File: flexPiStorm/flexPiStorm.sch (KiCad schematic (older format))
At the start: 9 parts, among them J1 Conn_01x04, J2 FPC-FFC-64, U1 MC68000

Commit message: Added LOGOs in the schematics, so the PCB will have them already. Run DRC for errors. Report only three (3) overlap for silkscreen and filled zones. No problem at all.
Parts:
- added L1: GNU GPL LOGO, RetroBitLab:Symbol_GNU-GPL_SilkScreen_Small, symbol AmigaComponents:LOGO
- added L2: KiCad LOGO Design, Symbol:KiCad-Logo2_6mm_SilkScreen, symbol AmigaComponents:LOGO
- added L3: PiStorm LOGO Design, RetroBitLab:PiStorm_32x6-NEG, symbol AmigaComponents:LOGO
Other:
- note added: "FLOPPY HEADER MOLEX 4 PIN CONNECTOR TYPE"
- note added: "LOGO FOR SILKSCREEN"
- note added: "MOUNTING HOLES 3.2mm"
- moved on the sheet: H1, H2, H3, H4
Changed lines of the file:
@@
 Sheet 1 1
 Title "Secondary CPU Flexible Relocator"
-Date "2021-06-25"
-Rev "0.1"
+Date "2021-06-27"
+Rev "0.2"
 Comp "RETROBIT LAB"
 Comment1 "FlexPiStorm"
@@
 L Mechanical:MountingHole H1
 U 1 1 60E64491
-P 8350 1550
-F 0 "H1" H 8450 1600 50  0000 L CNN
-F 1 "MountingHole" H 8450 1550 50  0000 L CNN
-F 2 "MountingHole:MountingHole_3.2mm_M3" H 8350 1550 50  0001 C CNN
-F 3 "~" H 8350 1550 50  0001 C CNN
-	1    8350 1550
-	1    0    0    -1
+P 9400 1500
+F 0 "H1" H 9500 1550 50  0000 L CNN
+F 1 "MountingHole" H 9500 1500 50  0000 L CNN
+F 2 "MountingHole:MountingHole_3.2mm_M3" H 9400 1500 50  0001 C CNN
+F 3 "~" H 9400 1500 50  0001 C CNN
+	1    9400 1500
+	0    -1   -1   0
 $EndComp
 $Comp
 L Mechanical:MountingHole H2
 U 1 1 60E64C09
-P 8350 1850
-F 0 "H2" H 8450 1900 50  0000 L CNN
-F 1 "MountingHole" H 8450 1850 50  0000 L CNN
-F 2 "MountingHole:MountingHole_3.2mm_M3" H 8350 1850 50  0001 C CNN
-F 3 "~" H 8350 1850 50  0001 C CNN
-	1    8350 1850
-	1    0    0    -1
+P 9700 1500
+F 0 "H2" H 9800 1550 50  0000 L CNN
+F 1 "MountingHole" H 9800 1500 50  0000 L CNN
+F 2 "MountingHole:MountingHole_3.2mm_M3" H 9700 1500 50  0001 C CNN
+F 3 "~" H 9700 1500 50  0001 C CNN
+	1    9700 1500
+	0    -1   -1   0
 $EndComp
 $Comp
 L Mechanical:MountingHole H3
 U 1 1 60E64DD7
-P 8350 2150
-F 0 "H3" H 8450 2200 50  0000 L CNN
-F 1 "MountingHole" H 8450 2150 50  0000 L CNN
-F 2 "MountingHole:MountingHole_3.2mm_M3" H 8350 2150 50  0001 C CNN
-F 3 "~" H 8350 2150 50  0001 C CNN
-	1    8350 2150
-	1    0    0    -1
+P 10000 1500
+F 0 "H3" H 10100 1550 50  0000 L CNN
+F 1 "MountingHole" H 10100 1500 50  0000 L CNN
+F 2 "MountingHole:MountingHole_3.2mm_M3" H 10000 1500 50  0001 C CNN
+F 3 "~" H 10000 1500 50  0001 C CNN
+	1    10000 1500
+	0    -1   -1   0
 $EndComp
 $Comp
 L Mechanical:MountingHole H4
 U 1 1 60E65040
-P 8350 2500
-F 0 "H4" H 8450 2550 50  0000 L CNN
-F 1 "MountingHole" H 8450 2500 50  0000 L CNN
-F 2 "MountingHole:MountingHole_3.2mm_M3" H 8350 2500 50  0001 C CNN
-F 3 "~" H 8350 2500 50  0001 C CNN
-	1    8350 2500
-	1    0    0    -1
+P 10350 1500
+F 0 "H4" H 10450 1550 50  0000 L CNN
+F 1 "MountingHole" H 10450 1500 50  0000 L CNN
+F 2 "MountingHole:MountingHole_3.2mm_M3" H 10350 1500 50  0001 C CNN
+F 3 "~" H 10350 1500 50  0001 C CNN
+	1    10350 1500
+	0    -1   -1   0
 $EndComp
 $Comp
@@
 Wire Wire Line
 	1150 3200 2000 3200
+Wire Notes Line
+	9050 800  9050 1750
+Wire Notes Line
+	9050 1750 10550 1750
+Wire Notes Line
+	10550 1750 10550 800
+Wire Notes Line
+	10550 800  9050 800
+Text Notes 9050 1900 0    79   ~ 16
+MOUNTING HOLES 3.2mm
+$Comp
+L AmigaComponents:LOGO L1
+U 1 1 60D96003
+P 9000 2550
+F 0 "L1" H 9150 2650 59  0000 L CNN
+F 1 "GNU GPL LOGO" H 9150 2500 59  0000 L CNN
+F 2 "RetroBitLab:Symbol_GNU-GPL_SilkScreen_Small" H 9000 2550 59  0001 C CNN
+F 3 "" H 9000 2550 59  0001 C CNN
+	1    9000 2550
+	1    0    0    -1
+$EndComp
+$Comp
+L AmigaComponents:LOGO L2
+U 1 1 60D96862
+P 9000 2850
+F 0 "L2" H 9150 2950 59  0000 L CNN
+F 1 "KiCad LOGO Design" H 9150 2800 59  0000 L CNN
+F 2 "Symbol:KiCad-Logo2_6mm_SilkScreen" H 9000 2850 59  0001 C CNN
+F 3 "" H 9000 2850 59  0001 C CNN
+	1    9000 2850
+	1    0    0    -1
+$EndComp
+$Comp
+L AmigaComponents:LOGO L3
+U 1 1 60D96C34
+P 9000 3150
+F 0 "L3" H 9150 3250 59  0000 L CNN
+F 1 "PiStorm LOGO Design" H 9150 3100 59  0000 L CNN
+F 2 "RetroBitLab:PiStorm_32x6-NEG" H 9000 3150 59  0001 C CNN
+F 3 "" H 9000 3150 59  0001 C CNN
+	1    9000 3150
+	1    0    0    -1
+$EndComp
+Wire Notes Line
+	9050 2300 9050 3350
+Wire Notes Line
+	9050 3350 10550 3350
+Wire Notes Line
+	10550 3350 10550 2300
+Wire Notes Line
+	10550 2300 9050 2300
+Text Notes 9050 3500 0    79   ~ 16
+LOGO FOR SILKSCREEN
+Text Notes 750  3700 0    79   ~ 16
+FLOPPY HEADER MOLEX 4 PIN CONNECTOR TYPE
 $EndSCHEMATC

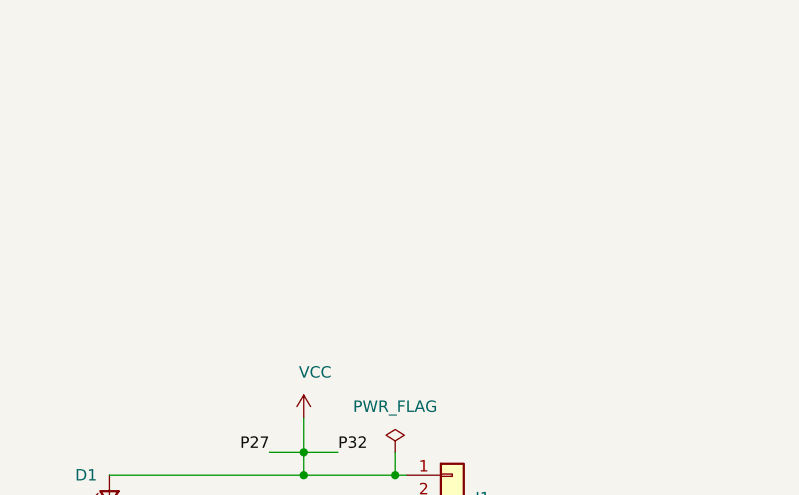
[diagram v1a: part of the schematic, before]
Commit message: Added bypass capacitors 10000pF Ceramics 1206 HandSolder
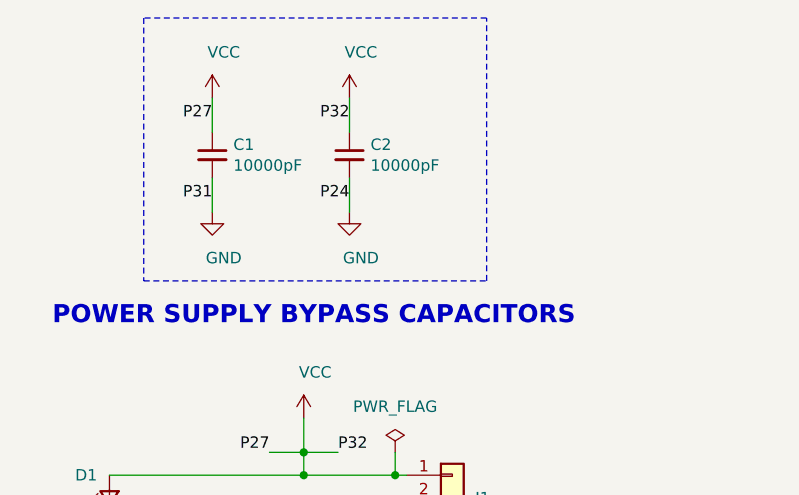
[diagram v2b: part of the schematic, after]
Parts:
- added C1, C2: 10000pF, Capacitor_SMD:C_1206_3216Metric_Pad1.33x1.80mm_HandSolder, symbol Device:C_Small
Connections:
- net GND: now also C1.2, C2.2
- net VCC: now also C1.1, C2.1
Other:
- note added: "POWER SUPPLY BYPASS CAPACITORS"
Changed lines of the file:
@@
 Sheet 1 1
 Title "Secondary CPU Flexible Relocator"
-Date "2021-06-27"
-Rev "0.2"
+Date "2021-06-28"
+Rev "0.3"
 Comp "RETROBIT LAB"
 Comment1 "FlexPiStorm"
@@
 Text Notes 750  3700 0    79   ~ 16
 FLOPPY HEADER MOLEX 4 PIN CONNECTOR TYPE
+$Comp
+L Device:C_Small C1
+U 1 1 60DA364B
+P 1600 1300
+F 0 "C1" H 1692 1346 50  0000 L CNN
+F 1 "10000pF" H 1692 1255 50  0000 L CNN
+F 2 "Capacitor_SMD:C_1206_3216Metric_Pad1.33x1.80mm_HandSolder" H 1600 1300 50  0001 C CNN
+F 3 "~" H 1600 1300 50  0001 C CNN
+	1    1600 1300
+	1    0    0    -1
+$EndComp
+Text Label 1600 1150 2    50   ~ 0
+P27
+Text Label 1600 1500 2    50   ~ 0
+P31
+$Comp
+L power:GND #PWR04
+U 1 1 60DA402B
+P 1600 1550
+F 0 "#PWR04" H 1600 1300 50  0001 C CNN
+F 1 "GND" H 1650 1350 50  0000 C CNN
+F 2 "" H 1600 1550 50  0001 C CNN
+F 3 "" H 1600 1550 50  0001 C CNN
+	1    1600 1550
+	1    0    0    -1
+$EndComp
+$Comp
+L power:VCC #PWR03
+U 1 1 60DA440B
+P 1600 1050
+F 0 "#PWR03" H 1600 900 50  0001 C CNN
+F 1 "VCC" H 1650 1250 50  0000 C CNN
+F 2 "" H 1600 1050 50  0001 C CNN
+F 3 "" H 1600 1050 50  0001 C CNN
+	1    1600 1050
+	1    0    0    -1
+$EndComp
+Wire Wire Line
+	1600 1050 1600 1200
+Wire Wire Line
+	1600 1400 1600 1550
+$Comp
+L Device:C_Small C2
+U 1 1 60DC5962
+P 2200 1300
+F 0 "C2" H 2292 1346 50  0000 L CNN
+F 1 "10000pF" H 2292 1255 50  0000 L CNN
+F 2 "Capacitor_SMD:C_1206_3216Metric_Pad1.33x1.80mm_HandSolder" H 2200 1300 50  0001 C CNN
+F 3 "~" H 2200 1300 50  0001 C CNN
+	1    2200 1300
+	1    0    0    -1
+$EndComp
+Text Label 2200 1150 2    50   ~ 0
+P32
+Text Label 2200 1500 2    50   ~ 0
+P24
+$Comp
+L power:GND #PWR06
+U 1 1 60DC5A8A
+P 2200 1550
+F 0 "#PWR06" H 2200 1300 50  0001 C CNN
+F 1 "GND" H 2250 1350 50  0000 C CNN
+F 2 "" H 2200 1550 50  0001 C CNN
+F 3 "" H 2200 1550 50  0001 C CNN
+	1    2200 1550
+	1    0    0    -1
+$EndComp
+$Comp
+L power:VCC #PWR05
+U 1 1 60DC5A94
+P 2200 1050
+F 0 "#PWR05" H 2200 900 50  0001 C CNN
+F 1 "VCC" H 2250 1250 50  0000 C CNN
+F 2 "" H 2200 1050 50  0001 C CNN
+F 3 "" H 2200 1050 50  0001 C CNN
+	1    2200 1050
+	1    0    0    -1
+$EndComp
+Wire Wire Line
+	2200 1050 2200 1200
+Wire Wire Line
+	2200 1400 2200 1550
+Wire Notes Line
+	1300 700  1300 1850
+Wire Notes Line
+	1300 1850 2800 1850
+Wire Notes Line
+	2800 1850 2800 700
+Wire Notes Line
+	2800 700  1300 700
+Text Notes 900  2050 0    79   ~ 16
+POWER SUPPLY BYPASS CAPACITORS
 $EndSCHEMATC

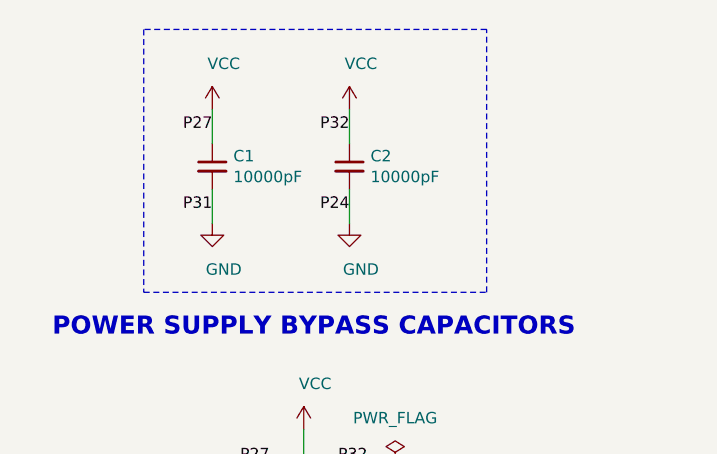
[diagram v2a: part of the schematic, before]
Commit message: Added a better filter for powersupply TANTALUM + CERAMIC (x2)
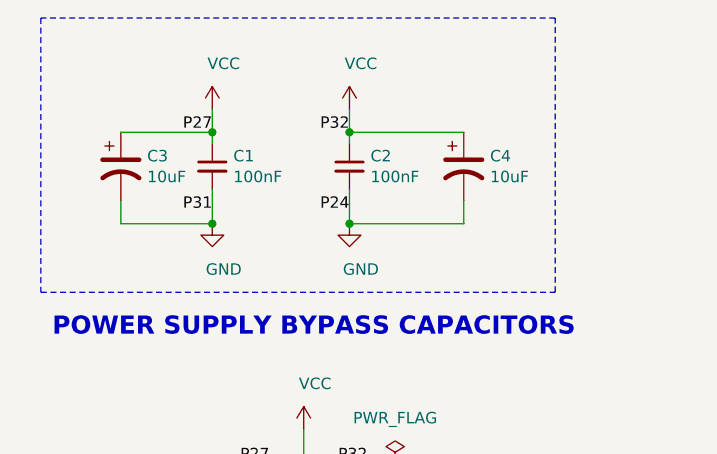
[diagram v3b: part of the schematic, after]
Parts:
- added C3, C4: 10uF, Capacitor_Tantalum_SMD:CP_EIA-3216-12_Kemet-S_Pad1.58x1.35mm_HandSolder, symbol Device:CP1
- C1, C2: value 10000pF -> 100nF
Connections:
- net GND: now also C3.2, C4.2
- net VCC: now also C3.1, C4.1
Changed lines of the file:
@@
 Sheet 1 1
 Title "Secondary CPU Flexible Relocator"
-Date "2021-06-28"
-Rev "0.3"
+Date "2021-06-29"
+Rev "0.4"
 Comp "RETROBIT LAB"
 Comment1 "FlexPiStorm"
@@
 P 1600 1300
 F 0 "C1" H 1692 1346 50  0000 L CNN
-F 1 "10000pF" H 1692 1255 50  0000 L CNN
+F 1 "100nF" H 1692 1255 50  0000 L CNN
 F 2 "Capacitor_SMD:C_1206_3216Metric_Pad1.33x1.80mm_HandSolder" H 1600 1300 50  0001 C CNN
 F 3 "~" H 1600 1300 50  0001 C CNN
@@
 $EndComp
 Wire Wire Line
-	1600 1050 1600 1200
+	1600 1050 1600 1150
 Wire Wire Line
 	1600 1400 1600 1550
@@
 P 2200 1300
 F 0 "C2" H 2292 1346 50  0000 L CNN
-F 1 "10000pF" H 2292 1255 50  0000 L CNN
+F 1 "100nF" H 2292 1255 50  0000 L CNN
 F 2 "Capacitor_SMD:C_1206_3216Metric_Pad1.33x1.80mm_HandSolder" H 2200 1300 50  0001 C CNN
 F 3 "~" H 2200 1300 50  0001 C CNN
@@
 $EndComp
 Wire Wire Line
-	2200 1050 2200 1200
+	2200 1050 2200 1150
 Wire Wire Line
 	2200 1400 2200 1550
-Wire Notes Line
-	1300 700  1300 1850
-Wire Notes Line
-	1300 1850 2800 1850
-Wire Notes Line
-	2800 1850 2800 700
-Wire Notes Line
-	2800 700  1300 700
 Text Notes 900  2050 0    79   ~ 16
 POWER SUPPLY BYPASS CAPACITORS
+$Comp
+L Device:CP1 C3
+U 1 1 60DB1E15
+P 1200 1300
+F 0 "C3" H 1315 1346 50  0000 L CNN
+F 1 "10uF" H 1315 1255 50  0000 L CNN
+F 2 "Capacitor_Tantalum_SMD:CP_EIA-3216-12_Kemet-S_Pad1.58x1.35mm_HandSolder" H 1200 1300 50  0001 C CNN
+F 3 "~" H 1200 1300 50  0001 C CNN
+	1    1200 1300
+	1    0    0    -1
+$EndComp
+$Comp
+L Device:CP1 C4
+U 1 1 60DB2236
+P 2700 1300
+F 0 "C4" H 2815 1346 50  0000 L CNN
+F 1 "10uF" H 2815 1255 50  0000 L CNN
+F 2 "Capacitor_Tantalum_SMD:CP_EIA-3216-12_Kemet-S_Pad1.58x1.35mm_HandSolder" H 2700 1300 50  0001 C CNN
+F 3 "~" H 2700 1300 50  0001 C CNN
+	1    2700 1300
+	1    0    0    -1
+$EndComp
+Wire Wire Line
+	1200 1150 1600 1150
+Connection ~ 1600 1150
+Wire Wire Line
+	1600 1150 1600 1200
+Wire Wire Line
+	1200 1450 1200 1550
+Wire Wire Line
+	1200 1550 1600 1550
+Connection ~ 1600 1550
+Wire Wire Line
+	2200 1550 2700 1550
+Wire Wire Line
+	2700 1550 2700 1450
+Connection ~ 2200 1550
+Wire Wire Line
+	2200 1150 2700 1150
+Connection ~ 2200 1150
+Wire Wire Line
+	2200 1150 2200 1200
+Wire Notes Line
+	850  650  850  1850
+Wire Notes Line
+	850  1850 3100 1850
+Wire Notes Line
+	3100 1850 3100 650
+Wire Notes Line
+	3100 650  850  650
 $EndSCHEMATC

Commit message: Modified for correct footprint CPU
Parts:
- U1: footprint RetroBitLab:MC68000_REPLACEMENT_FEMALE -> RetroBitLab:MC68000-SOCKET-RELOCATOR_FEMALE
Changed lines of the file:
@@
 Sheet 1 1
 Title "Secondary CPU Flexible Relocator"
-Date "2021-06-29"
-Rev "0.4"
+Date "2021-08-08"
+Rev "0.5"
 Comp "RETROBIT LAB"
 Comment1 "FlexPiStorm"
@@
 F 0 "U1" H 5500 4950 60  0000 C CNN
 F 1 "MC68000" H 5500 4850 60  0000 C CNN
-F 2 "RetroBitLab:MC68000_REPLACEMENT_FEMALE" H 5500 4790 60  0001 C CNN
+F 2 "RetroBitLab:MC68000-SOCKET-RELOCATOR_FEMALE" H 5500 4790 60  0001 C CNN
 F 3 "" H 4300 4550 60  0000 C CNN
 	1    5500 3000

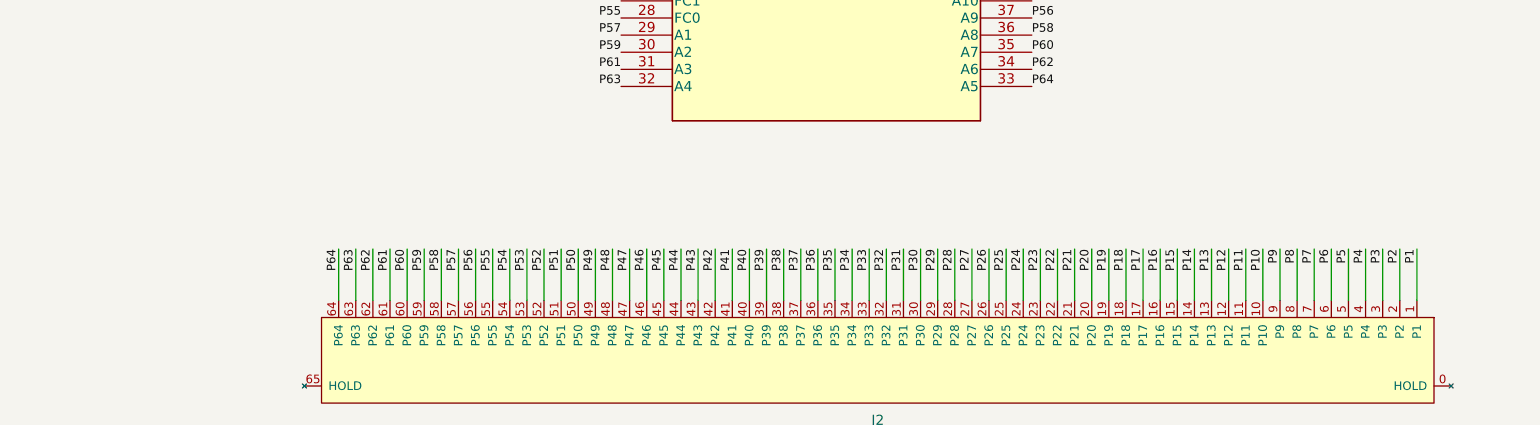
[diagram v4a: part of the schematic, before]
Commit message: Inverted ffc/fpc pinout for reverse mounting. Cable must be SAME SIDE
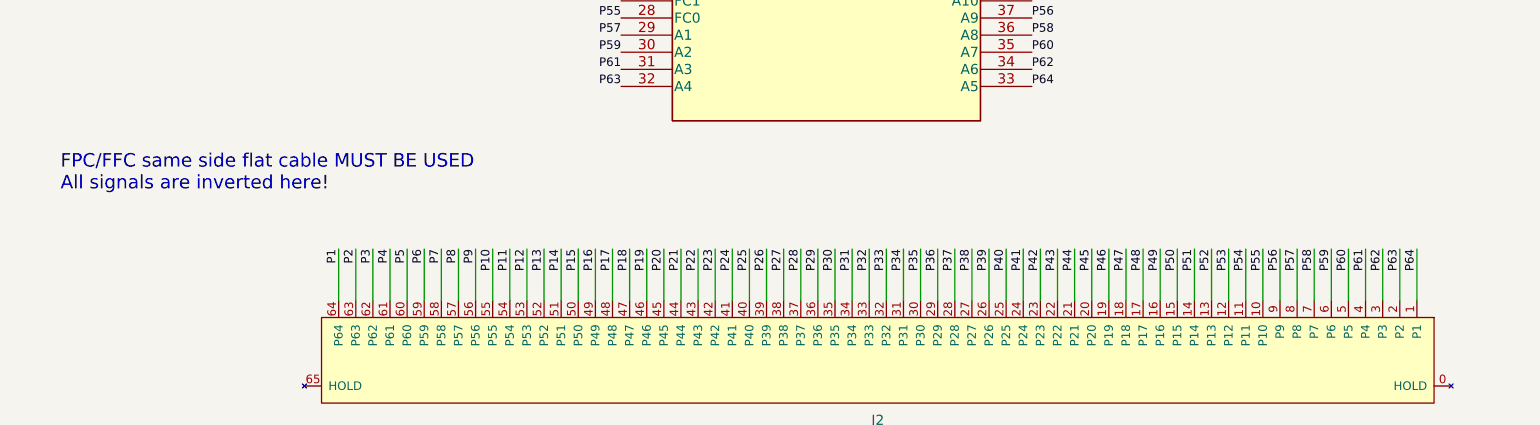
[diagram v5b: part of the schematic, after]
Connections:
- net GND: now also J2.34 (P34), J2.41 (P41); no longer J2.24 (P24), J2.31 (P31)
- net P1: now also J2.64 (P64); no longer J2.1 (P1)
- net P10: now also J2.55 (P55); no longer J2.10 (P10)
- net P11: now also J2.54 (P54); no longer J2.11 (P11)
- net P12: now also J2.53 (P53); no longer J2.12 (P12)
- net P13: now also J2.52 (P52); no longer J2.13 (P13)
- net P14: now also J2.51 (P51); no longer J2.14 (P14)
- net P15: now also J2.50 (P50); no longer J2.15 (P15)
- net P16: now also J2.49 (P49); no longer J2.16 (P16)
- net P17: now also J2.48 (P48); no longer J2.17 (P17)
- net P18: now also J2.47 (P47); no longer J2.18 (P18)
- net P19: now also J2.46 (P46); no longer J2.19 (P19)
- net P2: now also J2.63 (P63); no longer J2.2 (P2)
- net P20: now also J2.45 (P45); no longer J2.20 (P20)
- net P21: now also J2.44 (P44); no longer J2.21 (P21)
- net P22: now also J2.43 (P43); no longer J2.22 (P22)
- net P23: now also J2.42 (P42); no longer J2.23 (P23)
- net P25: now also J2.40 (P40); no longer J2.25 (P25)
- net P26: now also J2.39 (P39); no longer J2.26 (P26)
- net P28: now also J2.37 (P37); no longer J2.28 (P28)
- net P29: now also J2.36 (P36); no longer J2.29 (P29)
- net P3: now also J2.62 (P62); no longer J2.3 (P3)
- net P30: now also J2.35 (P35); no longer J2.30 (P30)
- net P33: now also J2.32 (P32); no longer J2.33 (P33)
- net P34: now also J2.31 (P31); no longer J2.34 (P34)
- net P35: now also J2.30 (P30); no longer J2.35 (P35)
- net P36: now also J2.29 (P29); no longer J2.36 (P36)
- net P37: now also J2.28 (P28); no longer J2.37 (P37)
- net P38: now also J2.27 (P27); no longer J2.38 (P38)
- net P39: now also J2.26 (P26); no longer J2.39 (P39)
- net P4: now also J2.61 (P61); no longer J2.4 (P4)
- net P40: now also J2.25 (P25); no longer J2.40 (P40)
- net P41: now also J2.24 (P24); no longer J2.41 (P41)
- net P42: now also J2.23 (P23); no longer J2.42 (P42)
- net P43: now also J2.22 (P22); no longer J2.43 (P43)
- net P44: now also J2.21 (P21); no longer J2.44 (P44)
- net P45: now also J2.20 (P20); no longer J2.45 (P45)
- net P46: now also J2.19 (P19); no longer J2.46 (P46)
- net P47: now also J2.18 (P18); no longer J2.47 (P47)
- net P48: now also J2.17 (P17); no longer J2.48 (P48)
- net P49: now also J2.16 (P16); no longer J2.49 (P49)
- net P5: now also J2.60 (P60); no longer J2.5 (P5)
- net P50: now also J2.15 (P15); no longer J2.50 (P50)
- net P51: now also J2.14 (P14); no longer J2.51 (P51)
- net P52: now also J2.13 (P13); no longer J2.52 (P52)
- net P53: now also J2.12 (P12); no longer J2.53 (P53)
- net P54: now also J2.11 (P11); no longer J2.54 (P54)
- net P55: now also J2.10 (P10); no longer J2.55 (P55)
- net P56: now also J2.9 (P9); no longer J2.56 (P56)
- net P57: now also J2.8 (P8); no longer J2.57 (P57)
- net P58: now also J2.7 (P7); no longer J2.58 (P58)
- net P59: now also J2.6 (P6); no longer J2.59 (P59)
- net P6: now also J2.59 (P59); no longer J2.6 (P6)
- net P60: now also J2.5 (P5); no longer J2.60 (P60)
- net P61: now also J2.4 (P4); no longer J2.61 (P61)
- net P62: now also J2.3 (P3); no longer J2.62 (P62)
- net P63: now also J2.2 (P2); no longer J2.63 (P63)
- net P64: now also J2.1 (P1); no longer J2.64 (P64)
- net P7: now also J2.58 (P58); no longer J2.7 (P7)
- net P8: now also J2.57 (P57); no longer J2.8 (P8)
- net P9: now also J2.56 (P56); no longer J2.9 (P9)
- net VCC: now also J2.33 (P33), J2.38 (P38); no longer J2.27 (P27), J2.32 (P32)
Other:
- note added: "FPC/FFC same side flat cable MUST BE USED\nAll signals are inverted here!"
